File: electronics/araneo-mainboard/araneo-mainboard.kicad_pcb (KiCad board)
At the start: 2 copper layers, 71.5 x 68.5 mm, 87 parts, among them IC1 TPS54302DDCR, IC2 BMI270, J1 GPIO2, J2 OLED, J3 GPIO1, SW2 SW, SW3 SW, U4 POWER, U5 PAM8403D

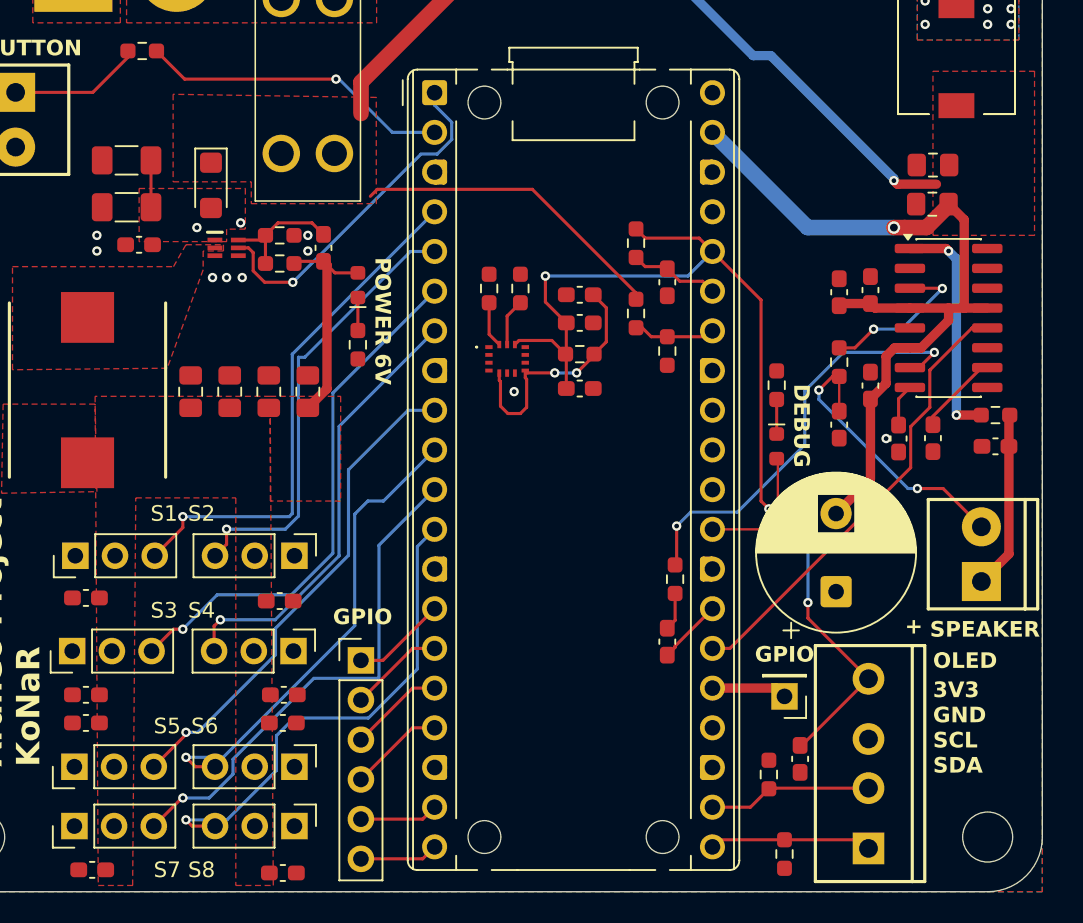
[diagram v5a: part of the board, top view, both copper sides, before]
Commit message: electronics: add magnetometer
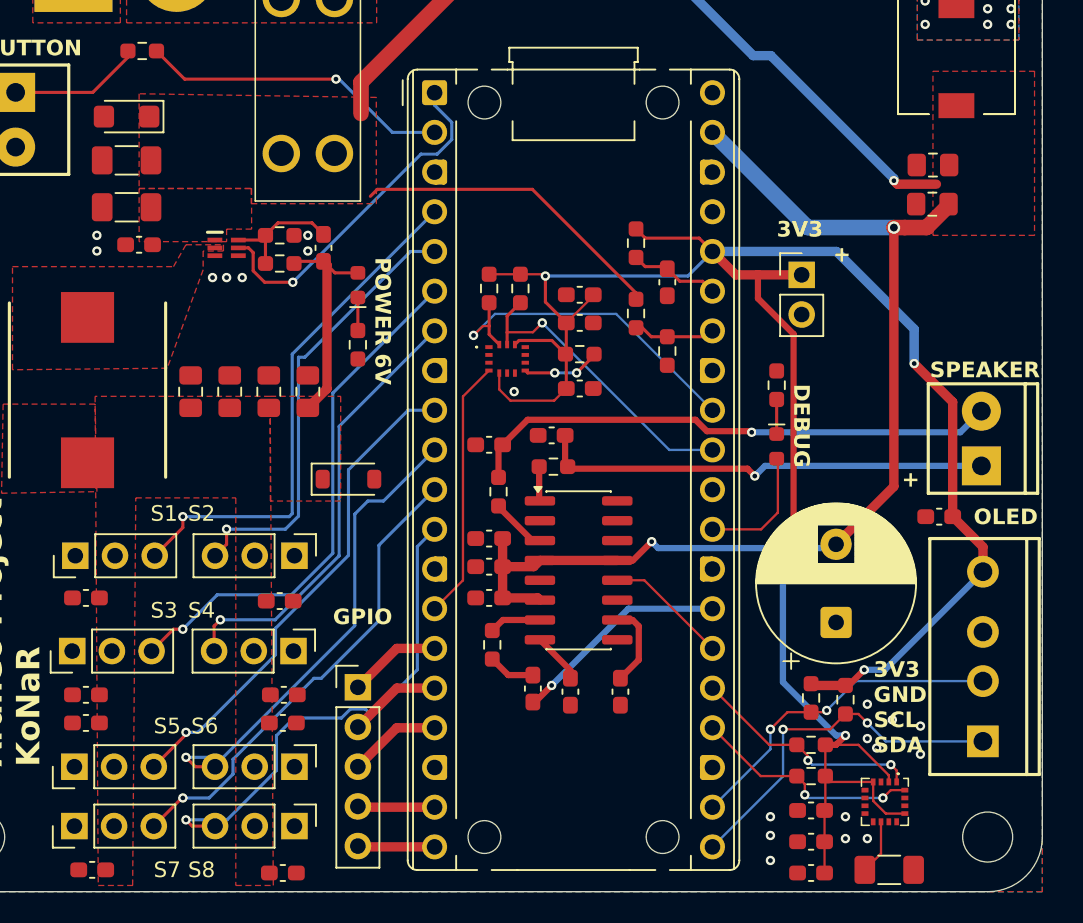
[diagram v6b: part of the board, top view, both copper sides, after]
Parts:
- removed J1: GPIO2, Connector_PinHeader_2.54mm:PinHeader_1x06_P2.54mm_Vertical
- added C2: 10u, Capacitor_SMD:C_1206_3216Metric_Pad1.33x1.80mm_HandSolder, F.Cu at (153.2, 102.6)
- added C3: 1u, Capacitor_SMD:C_0603_1608Metric_Pad1.08x0.95mm_HandSolder, F.Cu at (148.2, 98.8)
- added C4: 1u, Capacitor_SMD:C_0603_1608Metric_Pad1.08x0.95mm_HandSolder, F.Cu at (148.2, 100.8)
- added C5: 0.1u, Capacitor_SMD:C_0603_1608Metric_Pad1.08x0.95mm_HandSolder, F.Cu at (148.2, 102.8)
- added D1: SMF7V0A, Diode_SMD:D_SOD-123, F.Cu at (118.6, 77.6)
- added IC3: MMC5983MA, custom_footprints:MMC5983MA, F.Cu at (152.9, 98.2)
- added R3: 4.7k, Resistor_SMD:R_0603_1608Metric_Pad0.98x0.95mm_HandSolder, F.Cu at (148.2, 94.6)
- added R4: 4.7k, Resistor_SMD:R_0603_1608Metric_Pad0.98x0.95mm_HandSolder, F.Cu at (148.2, 96.6)
- added U6: 3V3, Connector_PinHeader_2.54mm:PinHeader_1x02_P2.54mm_Vertical, F.Cu at (147.6, 64.5)
- J3: value GPIO1 -> GPIO; footprint Connector_PinHeader_2.54mm:PinHeader_1x01_P2.54mm_Vertical -> Connector_PinHeader_2.54mm:PinHeader_1x05_P2.54mm_Vertical
- moved C16 30.1 mm to (127.6, 83.2), turned to 0 degrees
- moved U5 28.7 mm to (133.3, 83.4)
- moved FB1 28.5 mm to (131.7, 76.8)
- moved C11 28.4 mm to (131.6, 74.8)
- moved C15 27.9 mm to (127.6, 85.2), turned to 180 degrees
- moved C18 27.4 mm to (127.6, 81.4), turned to 0 degrees
- moved J3 27.3 mm to (119.2, 90.9), turned to 0 degrees
- moved C10 26.5 mm to (132.8, 91.2)
- moved C14 25.8 mm to (136.0, 91.2)
- moved FB2 23.3 mm to (128.2, 78.4), turned to 90 degrees
- moved C12 22.4 mm to (127.6, 75.4), turned to 0 degrees
- moved C19 17.9 mm to (156.4, 80.0), turned to 180 degrees
- moved R9 12.4 mm to (127.8, 88.2)
- moved R18 10.6 mm to (150.4, 91.7), turned to 90 degrees
- moved J2 10.0 mm to (159.2, 94.2)
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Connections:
- A1 pad 14: /GPIO10 -> /IMU_INT1
- A1 pad 24: /IMU_INT1 -> /MAG_SDA
- A1 pad 25: /GPIO19 -> /MAG_SCL
- C1 pad 2: Net-(IC2-VDD) -> +3V3
- C31 pad 1: Net-(D2-A2) -> +7.4V_F
- C32 pad 1: Net-(D2-A2) -> +7.4V_F
- C33 pad 1: Net-(D2-A2) -> +7.4V_F
- D2 pad 2: Net-(D2-A2) -> GND
- IC2 pad 13: /IMU/IMU_SCL -> /IMU_SDA
- IC2 pad 14: /IMU/IMU_SDA -> /IMU_SCL
- IC2 pad 4: /IMU/IMU_INT1 -> /IMU_INT1
- IC2 pad 5: Net-(IC2-VDD) -> +3V3
- J3 pad 1: /GPIO19 -> /GPIO11
- PS1 pad 1: Net-(D2-A2) -> +7.4V_F
- R1 pad 1: GND -> +3V3
- R1 pad 2: /IMU/IMU_SCL -> /IMU_SDA
- R18 pad 2: GND -> +3V3
- R19 pad 2: GND -> +3V3
- R2 pad 1: GND -> +3V3
- R2 pad 2: /IMU/IMU_SDA -> /IMU_SCL
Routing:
- net +3V3: track 66.0 -> 147.7 mm, vias 3 -> 5
- net Net-(U5-INL): track 27.6 -> 3.33 mm, vias 2 -> 0
- net /IMU_SCL: track 0.00 -> 22.6 mm, vias 0 -> 1
- net /SHDN: track 29.0 -> 7.90 mm
- net /IMU_SDA: track 0.00 -> 19.8 mm, vias 0 -> 1
- net Net-(C11-Pad2): track 11.4 -> 29.1 mm, vias 0 -> 1
- net /IMU_INT1: track 0.00 -> 16.7 mm
- net +5V: track 88.5 -> 105.0 mm, vias 3 -> 4
- net Net-(C12-Pad2): track 18.3 -> 34.4 mm, vias 2 -> 1
- net /MAG_SCL: track 0.00 -> 14.9 mm, vias 0 -> 2
- net /MAG_SDA: track 0.00 -> 14.8 mm, vias 0 -> 2
- net /SDA_OLED: track 10.4 -> 23.3 mm, vias 0 -> 2
- net Net-(U5-LOUT+): track 14.8 -> 2.21 mm, vias 2 -> 0
- net Net-(IC2-VDD): track 16.1 -> 5.01 mm
- net /SCL_OLED: track 11.3 -> 21.4 mm, vias 0 -> 2
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- removed copper zone on F.Cu, net Net-(D2-A2)
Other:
- board text added: "3V3"

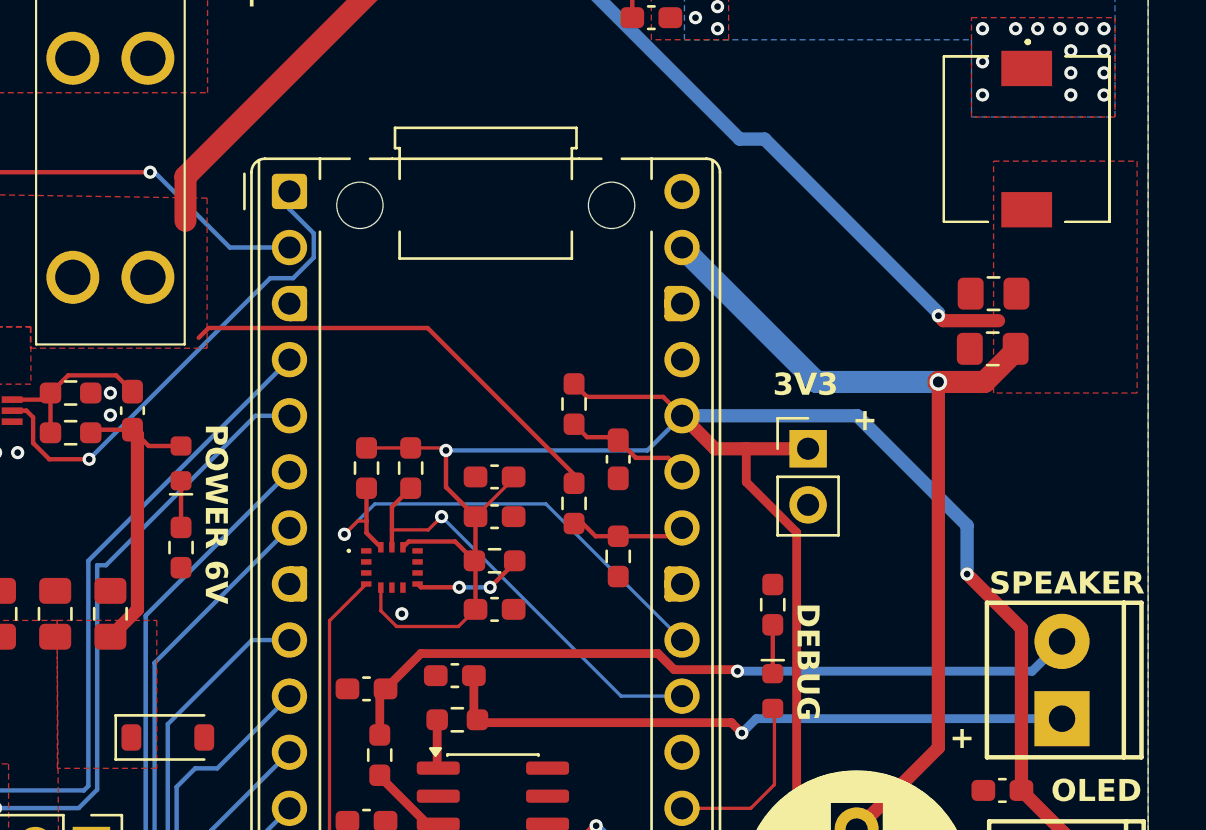
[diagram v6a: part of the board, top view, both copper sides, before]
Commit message: electronics: add 100n capacitors
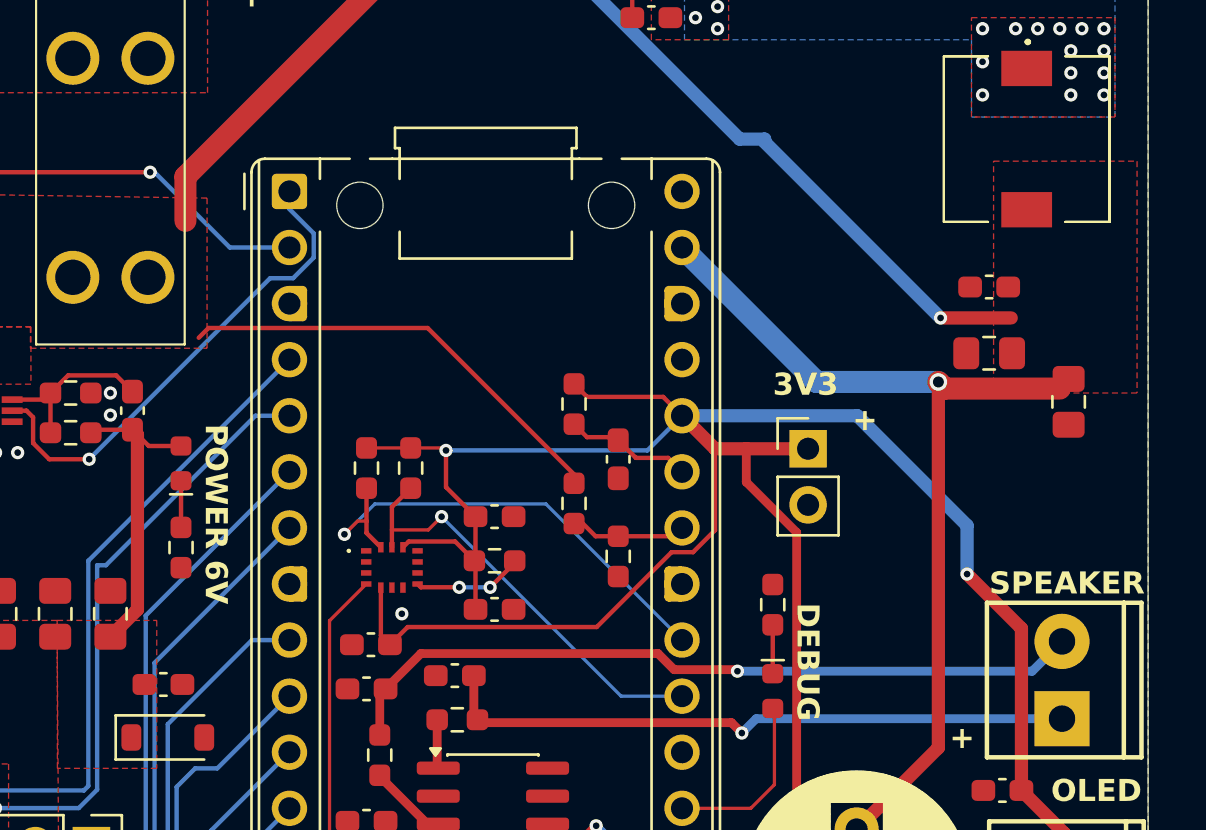
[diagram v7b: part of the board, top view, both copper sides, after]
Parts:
- added C44: 100n, Capacitor_SMD:C_0603_1608Metric_Pad1.08x0.95mm_HandSolder, F.Cu at (155.8, 57.2)
- added C45: 100n, Capacitor_SMD:C_0603_1608Metric_Pad1.08x0.95mm_HandSolder, F.Cu at (118.4, 75.2)
- moved C1 9.44 mm to (127.8, 73.4)
- moved C30 4.19 mm to (159.4, 62.4), turned to -90 degrees
- moved C29 2.71 mm to (155.8, 60.2)
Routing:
- net +3V3: track 147.7 -> 162.5 mm
- net +5V: track 105.0 -> 106.9 mm

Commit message: electronics: change capacitor footprint
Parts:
- C41: footprint Capacitor_SMD:C_0603_1608Metric_Pad1.08x0.95mm_HandSolder -> Capacitor_SMD:C_0805_2012Metric_Pad1.18x1.45mm_HandSolder
